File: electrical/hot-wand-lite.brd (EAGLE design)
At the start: 112 x 72 mm, 89 parts, among them IC1 12V R-78K12-2.0, IC2 AMS1117-5.0, Q1 NCHAN, Q2 SIS862ADN-T1-GE3, Q3 DMTH64M2LPDWQ-13, Q4 2N7002K, Q5 SIS862ADN-T1-GE3, U1 SEEED-XIAO-SAMD21-TH-LOCKING, U2 1EDN8511BXUSA1, U3 LM74700QDBVTQ1, U4 AP53781

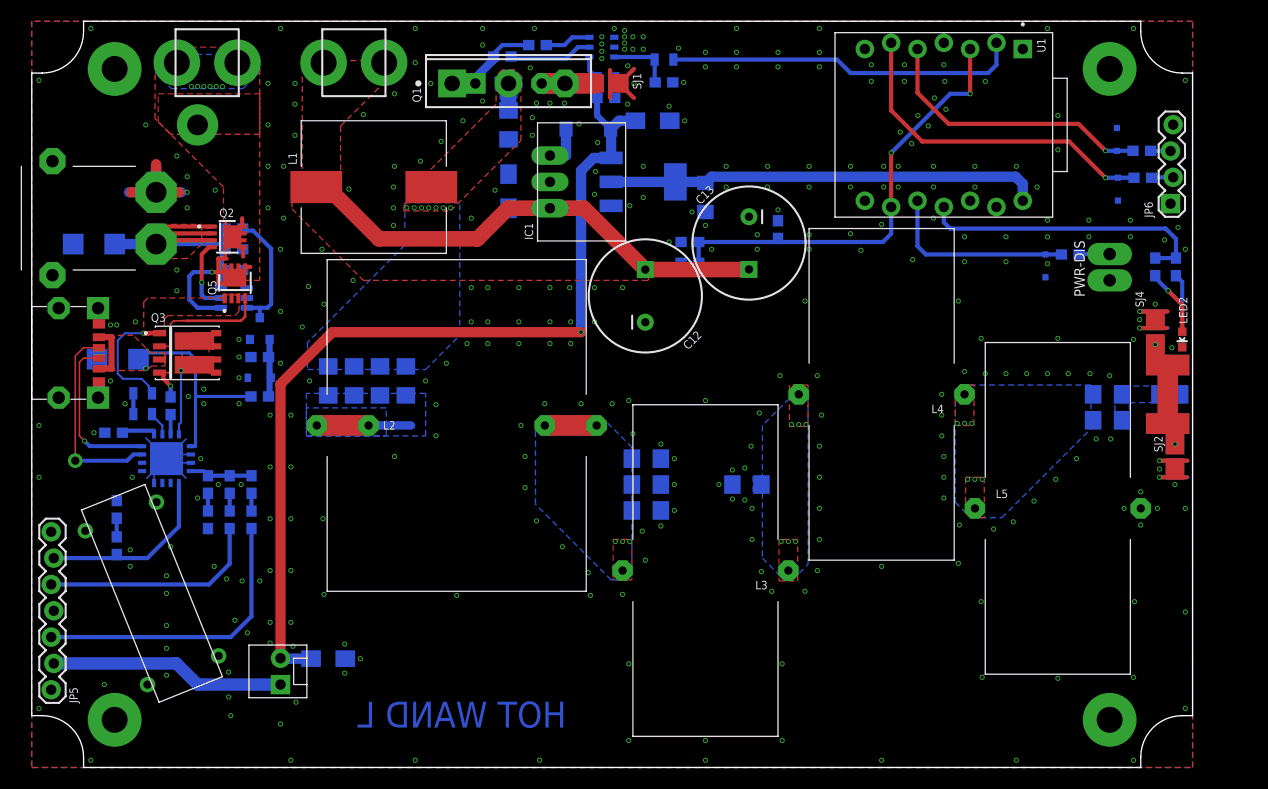
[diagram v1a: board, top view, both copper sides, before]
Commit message: lite version ready to order, corrected QFN16 footprint
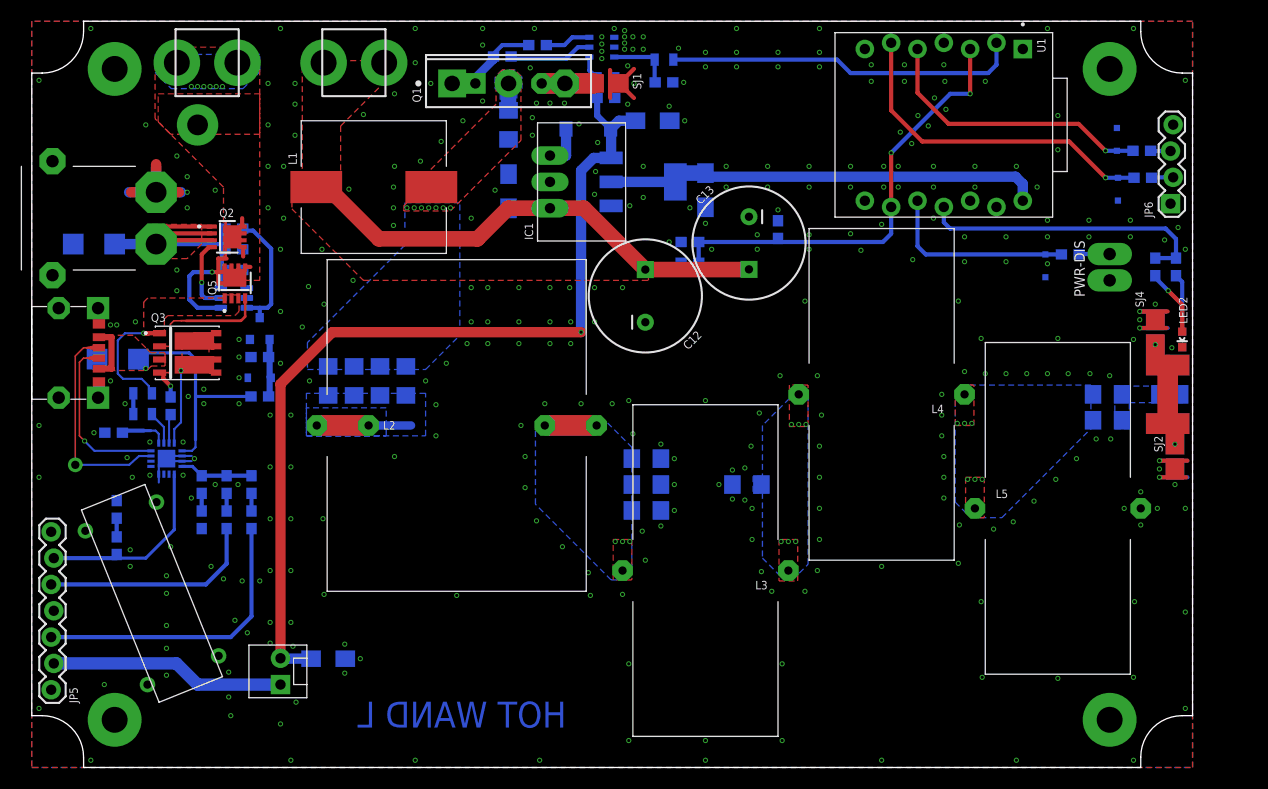
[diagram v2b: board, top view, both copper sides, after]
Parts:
- C16: device hot-wand:EIA3216 -> hot-wand:EIA3216-KIT
- U4: device hot-wand:QFN-16 -> hot-wand:QFN3030-16
- moved C16 0.70 mm to (65.0, 55.7)
- moved R15 0.60 mm to (16.4, 27.3)
- moved R16 0.60 mm to (16.4, 23.9)
- moved R19 0.30 mm to (18.8, 27.3)
- moved R20 0.30 mm to (18.8, 23.9)
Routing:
- net GND: track 58.6 -> 45.9 mm, vias 341 -> 346
- net N$44: track 19.4 -> 22.6 mm
- net N$41: track 15.6 -> 18.3 mm
- net N$38: track 3.48 -> 4.60 mm
- net N$39: track 27.8 -> 28.9 mm
- net N$35: track 18.1 -> 19.1 mm
- net N$42: track 6.05 -> 7.07 mm
- net N$40: track 2.36 -> 3.28 mm
- net N$36: track 1.90 -> 2.81 mm
- net 5V: track 42.0 -> 42.8 mm
- net USB-I-SEL: track 17.9 -> 18.5 mm

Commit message: changed lite v reading divider
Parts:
- R21: value 4K7 -> 100K
- R22: value 470Ω -> 4K7
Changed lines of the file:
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@@
 <attribute name="DNP" value="1" x="41.5" y="5.1" size="1.778" layer="28" rot="MR0" display="off"/>
 </element>
-<element name="R22" library="hot-wand" package="0603-RES" value="470Ω" x="63.5" y="50.7" smashed="yes" rot="MR0">
-<attribute name="JLCPARTNUM" value="C23179" x="63.5" y="50.7" size="0.8128" layer="28" font="fixed" rot="MR0" display="off"/>
+<element name="R22" library="hot-wand" package="0603-RES" value="4K7" x="63.5" y="50.7" smashed="yes" rot="MR0">
+<attribute name="JLCPARTNUM" value="C23162" x="63.5" y="50.7" size="0.8128" layer="28" font="fixed" rot="MR0" display="off"/>
 <attribute name="NAME" x="65.111" y="51.538" size="0.8128" layer="26" font="fixed" rot="MR180"/>
 <attribute name="VALUE" x="65.084" y="50.443" size="0.8128" layer="28" font="fixed" rot="MR180"/>
 </element>
-<element name="R21" library="hot-wand" package="0603-RES" value="4K7" x="63.5" y="48.7" smashed="yes" rot="MR0">
-<attribute name="JLCPARTNUM" value="C23162" x="63.5" y="48.7" size="0.8128" layer="28" font="fixed" rot="MR0" display="off"/>
+<element name="R21" library="hot-wand" package="0603-RES" value="100K" x="63.5" y="48.7" smashed="yes" rot="MR0">
+<attribute name="JLCPARTNUM" value="C25803" x="63.5" y="48.7" size="0.8128" layer="28" font="fixed" rot="MR0" display="off"/>
 <attribute name="NAME" x="62.211" y="47.838" size="0.8128" layer="26" font="fixed" rot="MR180"/>
 <attribute name="VALUE" x="65.084" y="48.543" size="0.8128" layer="28" font="fixed" rot="MR180"/>

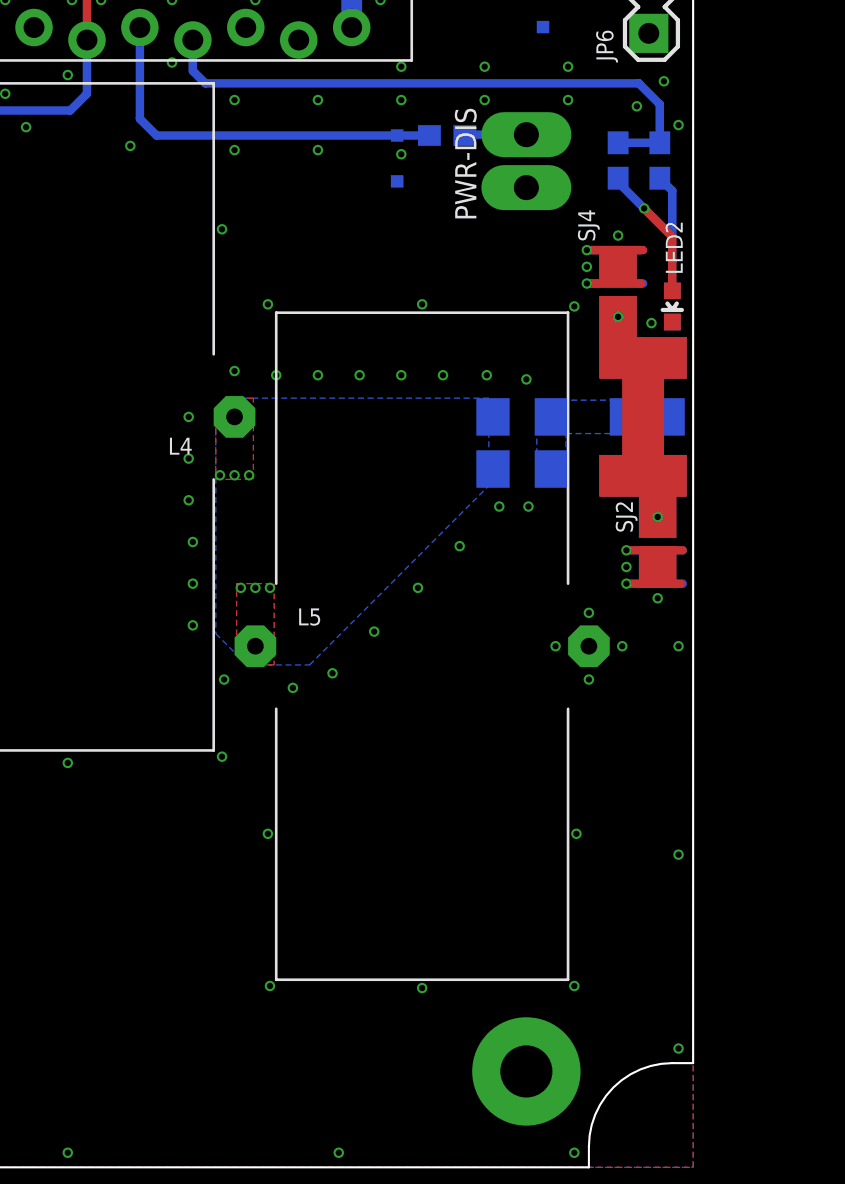
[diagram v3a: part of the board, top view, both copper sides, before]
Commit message: added a power switch to lite pcb
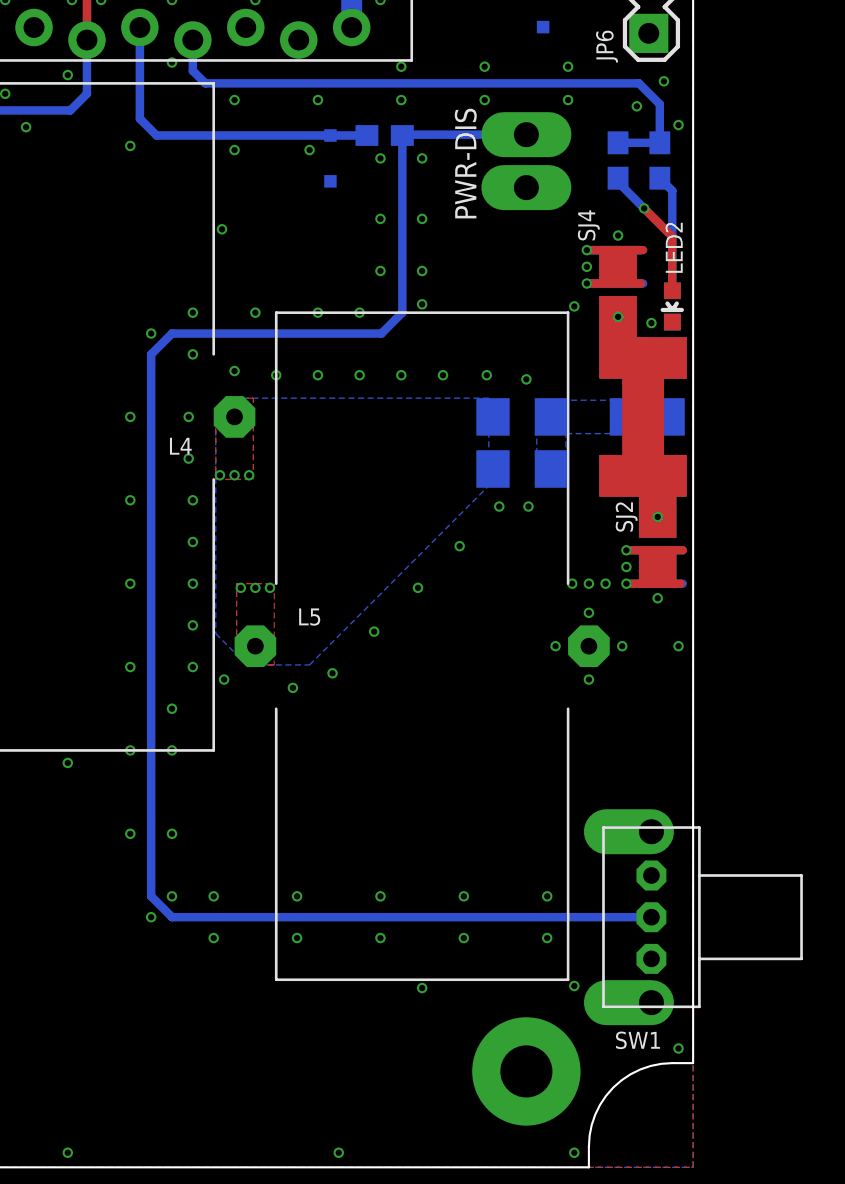
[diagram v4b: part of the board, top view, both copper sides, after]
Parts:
- added SW1: (no value), hot-wand:SWITCH-SLW-864574-5A-RA-N-D
- moved TVS6 3.20 mm to (94.6, 48.4)
- moved R25 3.00 mm to (97.2, 49.5)
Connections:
- net GND: now also SW1.M1, SW1.M2, SW1.R
- net N$21: now also SW1.C
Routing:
- net N$21: track 2.97 -> 77.7 mm
- net PWR-DIS: track 18.6 -> 15.6 mm
- net GND: vias 346 -> 376
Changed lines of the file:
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@@
 <layer number="27" name="tValues" color="7" fill="1" visible="yes" active="yes"/>
 <layer number="28" name="bValues" color="7" fill="1" visible="yes" active="yes"/>
-<layer number="29" name="tStop" color="7" fill="3" visible="no" active="yes"/>
+<layer number="29" name="tStop" color="7" fill="3" visible="yes" active="yes"/>
 <layer number="30" name="bStop" color="7" fill="6" visible="no" active="yes"/>
 <layer number="31" name="tCream" color="7" fill="4" visible="no" active="yes"/>
@@
 <attribute name="VALUE" x="102.4" y="59.5" size="1.27" layer="28" rot="MR90"/>
 </element>
-<element name="TVS6" library="hot-wand" package="SOD323-R" value="" x="97.8" y="48.4" smashed="yes" rot="MR270">
-<attribute name="JLCPARTNUM" value="C840638" x="97.8" y="48.4" size="1.016" layer="28" rot="MR270" display="off"/>
-<attribute name="NAME" x="96.8" y="49.5" size="0.8128" layer="26" rot="MR270"/>
-<attribute name="VALUE" x="100.1" y="49.5" size="1.27" layer="28" rot="MR270"/>
+<element name="TVS6" library="hot-wand" package="SOD323-R" value="" x="94.6" y="48.4" smashed="yes" rot="MR270">
+<attribute name="JLCPARTNUM" value="C840638" x="94.6" y="48.4" size="1.016" layer="28" rot="MR270" display="off"/>
+<attribute name="NAME" x="93.6" y="49.5" size="0.8128" layer="26" rot="MR270"/>
+<attribute name="VALUE" x="96.9" y="49.5" size="1.27" layer="28" rot="MR270"/>
 </element>
 <element name="R23" library="hot-wand" package="0603-RES" value="470Ω" x="107.2" y="56.9" smashed="yes" rot="MR180">
@@
 <attribute name="VALUE" x="108.416" y="61.457" size="0.8128" layer="28" font="vector" rot="MR0"/>
 </element>
-<element name="R25" library="hot-wand" package="0603-RES" value="470Ω" x="100.2" y="49.5" smashed="yes" rot="MR180">
-<attribute name="JLCPARTNUM" value="C23179" x="100.2" y="49.5" size="0.8128" layer="28" rot="MR180" display="off"/>
-<attribute name="NAME" x="101.189" y="50.262" size="0.8128" layer="26" font="vector" rot="MR0"/>
-<attribute name="VALUE" x="101.316" y="51.257" size="0.8128" layer="28" font="vector" rot="MR0"/>
+<element name="R25" library="hot-wand" package="0603-RES" value="470Ω" x="97.2" y="49.5" smashed="yes" rot="MR180">
+<attribute name="JLCPARTNUM" value="C23179" x="97.2" y="49.5" size="0.8128" layer="28" rot="MR180" display="off"/>
+<attribute name="NAME" x="98.189" y="50.262" size="0.8128" layer="26" font="vector" rot="MR0"/>
+<attribute name="VALUE" x="98.316" y="51.257" size="0.8128" layer="28" font="vector" rot="MR0"/>
+</element>
+<element name="SW1" library="hot-wand" package="SWITCH-SLW-864574-5A-RA-N-D" value="" x="110" y="12" smashed="yes" rot="R270">
+<attribute name="NAME" x="110.5" y="6.5" size="0.8128" layer="25" rot="R180"/>
+<attribute name="JLC-DNP" value="1" x="110" y="12" size="1.778" layer="27" rot="R270" display="off"/>
+<attribute name="PARTNUM" value="SLW-864574-5A-RA-N-D" x="110" y="12" size="1.778" layer="27" rot="R270" display="off"/>
 </element>
 </elements>
@@
 <via x="88" y="28" extent="1-16" drill="0.3" shape="octagon"/>
 <via x="88" y="30" extent="1-16" drill="0.3" shape="octagon"/>
-<via x="87.8" y="32" extent="1-16" drill="0.3" shape="octagon"/>
+<via x="88" y="32" extent="1-16" drill="0.3" shape="octagon"/>
 <via x="87.8" y="34" extent="1-16" drill="0.3" shape="octagon"/>
 <via x="87.8" y="36" extent="1-16" drill="0.3" shape="octagon"/>
@@
 <via x="106.3" y="0.7" extent="1-16" drill="0.3" shape="octagon"/>
 <via x="111.3" y="25" extent="1-16" drill="0.3" shape="octagon"/>
-<via x="111.3" y="15" extent="1-16" drill="0.3" shape="octagon"/>
 <via x="5.7" y="0.7" extent="1-16" drill="0.3" shape="octagon"/>
 <via x="0.7" y="5.7" extent="1-16" drill="0.3" shape="octagon"/>
@@
 <via x="74.6" y="45" extent="1-16" drill="0.3" shape="octagon"/>
 <via x="89.4" y="45" extent="1-16" drill="0.3" shape="octagon"/>
-<via x="89.4" y="19.7" extent="1-16" drill="0.3" shape="octagon"/>
+<via x="89" y="13" extent="1-16" drill="0.3" shape="octagon"/>
 <via x="82" y="19.4" extent="1-16" drill="0.3" shape="octagon"/>
 <via x="82" y="52.4" extent="1-16" drill="0.3" shape="octagon"/>
-<via x="91.6" y="41.4" extent="1-16" drill="0.3" shape="octagon"/>
+<via x="91" y="41" extent="1-16" drill="0.3" shape="octagon"/>
 <via x="99" y="41.4" extent="1-16" drill="0.3" shape="octagon"/>
 <via x="106.3" y="41.3" extent="1-16" drill="0.3" shape="octagon"/>
-<via x="91.6" y="16" extent="1-16" drill="0.3" shape="octagon"/>
-<via x="91.7" y="8.7" extent="1-16" drill="0.3" shape="octagon"/>
 <via x="99" y="8.6" extent="1-16" drill="0.3" shape="octagon"/>
 <via x="106.3" y="8.7" extent="1-16" drill="0.3" shape="octagon"/>
-<via x="106.4" y="16" extent="1-16" drill="0.3" shape="octagon"/>
 <via x="65" y="35.4" extent="1-16" drill="0.3" shape="octagon"/>
 <via x="65" y="2.6" extent="1-16" drill="0.3" shape="octagon"/>
@@
 <via x="28.2" y="16.7" extent="1-16" drill="0.3" shape="octagon"/>
 <contactref element="JP4" pad="1"/>
-<via x="98" y="48.6" extent="1-16" drill="0.3" shape="octagon"/>
-<via x="94" y="48.8" extent="1-16" drill="0.3" shape="octagon"/>
+<via x="97" y="48.4" extent="1-16" drill="0.3" shape="octagon"/>
+<via x="93.6" y="48.8" extent="1-16" drill="0.3" shape="octagon"/>
 <via x="90" y="48.8" extent="1-16" drill="0.3" shape="octagon"/>
 <via x="85" y="49" extent="1-16" drill="0.3" shape="octagon"/>
@@
 <via x="14.6" y="28.2" extent="1-16" drill="0.3" shape="octagon"/>
 <via x="9.2" y="29.9" extent="1-16" drill="0.3" shape="octagon"/>
+<contactref element="SW1" pad="R"/>
+<contactref element="SW1" pad="M1"/>
+<contactref element="SW1" pad="M2"/>
+<via x="99" y="48.4" extent="1-16" drill="0.3" shape="octagon"/>
+<via x="85" y="36" extent="1-16" drill="0.3" shape="octagon"/>
+<via x="85" y="32" extent="1-16" drill="0.3" shape="octagon"/>
+<via x="85" y="28" extent="1-16" drill="0.3" shape="octagon"/>
+<via x="85" y="24" extent="1-16" drill="0.3" shape="octagon"/>
+<via x="86" y="40" extent="1-16" drill="0.3" shape="octagon"/>
+<via x="88" y="39" extent="1-16" drill="0.3" shape="octagon"/>
+<via x="88" y="41" extent="1-16" drill="0.3" shape="octagon"/>
+<via x="88" y="24" extent="1-16" drill="0.3" shape="octagon"/>
+<via x="85" y="20" extent="1-16" drill="0.3" shape="octagon"/>
+<via x="87" y="20" extent="1-16" drill="0.3" shape="octagon"/>
+<via x="89" y="11" extent="1-16" drill="0.3" shape="octagon"/>
+<via x="93" y="11" extent="1-16" drill="0.3" shape="octagon"/>
+<via x="97" y="11" extent="1-16" drill="0.3" shape="octagon"/>
+<via x="101" y="11" extent="1-16" drill="0.3" shape="octagon"/>
+<via x="105" y="11" extent="1-16" drill="0.3" shape="octagon"/>
+<via x="93" y="13" extent="1-16" drill="0.3" shape="octagon"/>
+<via x="97" y="13" extent="1-16" drill="0.3" shape="octagon"/>
+<via x="101" y="13" extent="1-16" drill="0.3" shape="octagon"/>
+<via x="105" y="13" extent="1-16" drill="0.3" shape="octagon"/>
+<via x="94" y="41" extent="1-16" drill="0.3" shape="octagon"/>
+<via x="96" y="41" extent="1-16" drill="0.3" shape="octagon"/>
+<via x="97" y="43" extent="1-16" drill="0.3" shape="octagon"/>
+<via x="99" y="43" extent="1-16" drill="0.3" shape="octagon"/>
+<via x="99" y="45.5" extent="1-16" drill="0.3" shape="octagon"/>
+<via x="97" y="45.5" extent="1-16" drill="0.3" shape="octagon"/>
+<via x="106.2" y="28" extent="1-16" drill="0.3" shape="octagon"/>
+<via x="107" y="28" extent="1-16" drill="0.3" shape="octagon"/>
+<via x="107.8" y="28" extent="1-16" drill="0.3" shape="octagon"/>
+<via x="85" y="16" extent="1-16" drill="0.3" shape="octagon"/>
+<via x="87" y="16" extent="1-16" drill="0.3" shape="octagon"/>
+<via x="87" y="13" extent="1-16" drill="0.3" shape="octagon"/>
+<via x="86" y="12" extent="1-16" drill="0.3" shape="octagon"/>
+<via x="87" y="22" extent="1-16" drill="0.3" shape="octagon"/>
 </signal>
 <signal name="+24V">
@@
 <contactref element="TVS6" pad="C"/>
 <contactref element="R25" pad="1"/>
-<wire x1="99.35" y1="49.5" x2="97.8" y2="49.5" width="0.4064" layer="16"/>
-<wire x1="97.8" y1="49.5" x2="86.26" y2="49.5" width="0.4064" layer="16"/>
+<wire x1="96.35" y1="49.5" x2="94.6" y2="49.5" width="0.4064" layer="16"/>
+<wire x1="94.6" y1="49.5" x2="86.26" y2="49.5" width="0.4064" layer="16"/>
 <wire x1="86.26" y1="49.5" x2="85.46" y2="50.3" width="0.4064" layer="16"/>
 <wire x1="85.46" y1="50.3" x2="85.46" y2="54.68" width="0.4064" layer="16"/>
@@
 <contactref element="JP4" pad="2"/>
 <contactref element="R25" pad="2"/>
-<wire x1="104" y1="49.54" x2="101.09" y2="49.54" width="0.4064" layer="16"/>
-<wire x1="101.09" y1="49.54" x2="101.05" y2="49.5" width="0.4064" layer="16"/>
+<wire x1="104" y1="49.54" x2="98.19" y2="49.54" width="0.4064" layer="16"/>
+<wire x1="98.19" y1="49.54" x2="98.05" y2="49.5" width="0.4064" layer="16"/>
+<contactref element="SW1" pad="C"/>
+<wire x1="110" y1="12" x2="87" y2="12" width="0.4064" layer="16"/>
+<wire x1="87" y1="12" x2="86" y2="13" width="0.4064" layer="16"/>
+<wire x1="86" y1="13" x2="86" y2="39" width="0.4064" layer="16"/>
+<wire x1="86" y1="39" x2="87" y2="40" width="0.4064" layer="16"/>
+<wire x1="87" y1="40" x2="97.05" y2="40" width="0.4064" layer="16"/>
+<wire x1="97.05" y1="40" x2="98.05" y2="41" width="0.4064" layer="16"/>
+<wire x1="98.05" y1="41" x2="98.05" y2="49.5" width="0.4064" layer="16"/>
 </signal>
 </signals>
